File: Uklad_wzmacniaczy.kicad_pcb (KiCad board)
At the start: 4 copper layers, 80 x 120 mm, 85 parts, among them J1 SJ1-3523N, J2 MEM2080-00-128-00-A, J3 Conn_01x10_Pin, U1 OPA2388IDR, U10 AD5162BRMZ10-RL7, U11 AD5162BRMZ10-RL7, U12 LT3094EMSE-TRPBF, U13 Nucleo-H755ZIQ-Morpho, U14 TPS61236PRWLR, U15 LD1117S50TR_SOT223, U2 REF2033QDDCRQ1, U3 AD8421ARMZ, U4 OPA388IDR, U5 AD8421ARMZ, U6 TPD4E1B06DRLR, U7 AD5162BRMZ10-RL7, U8 LT3042EMSE-TRPBF, U9 TPS65135RTER

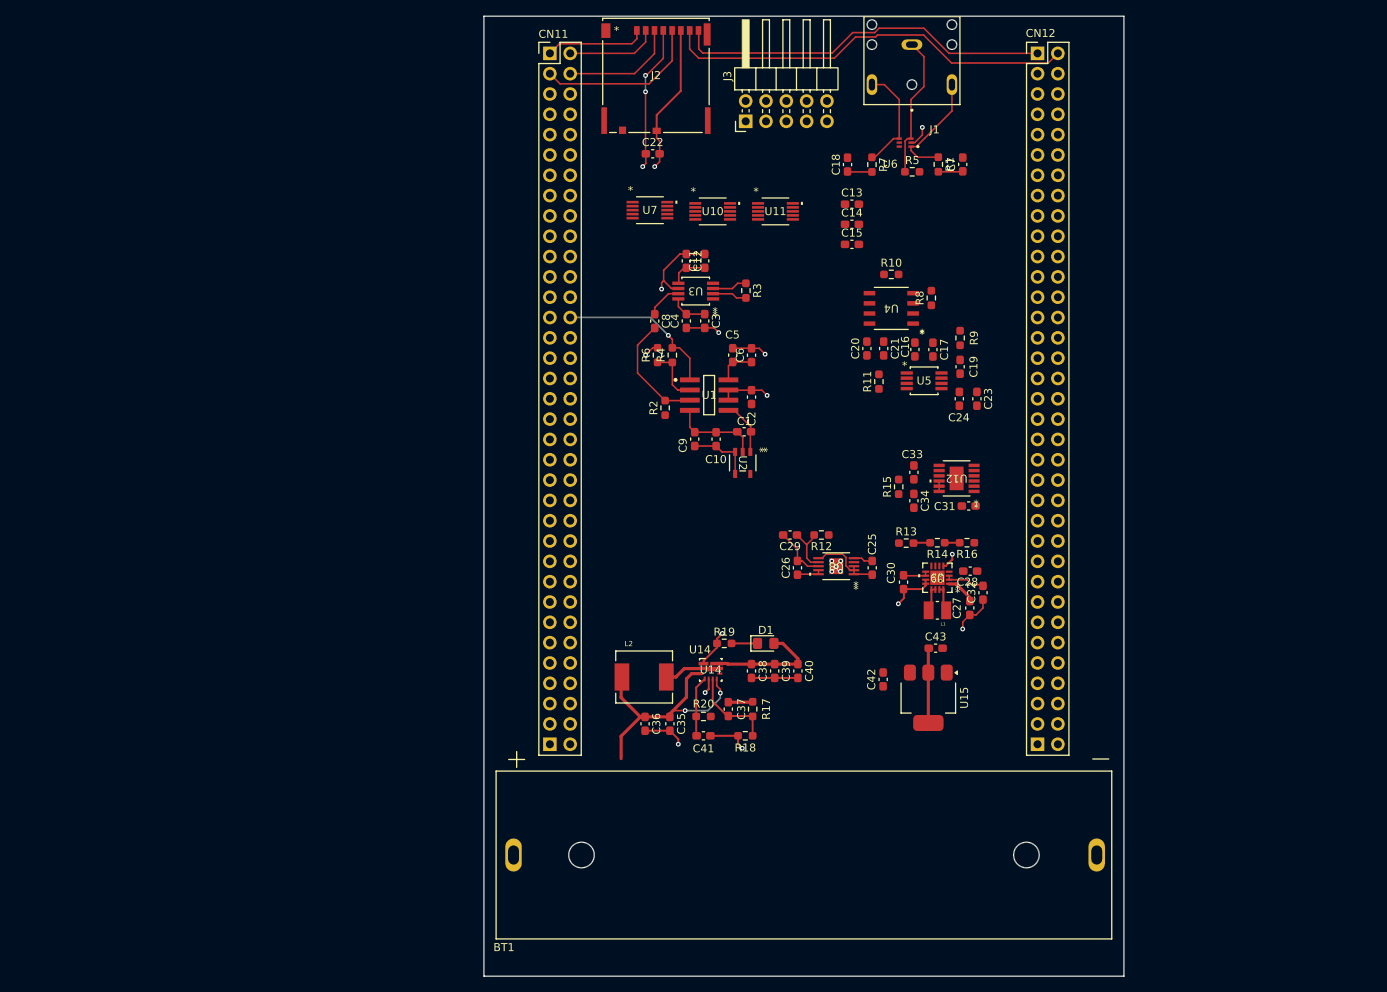
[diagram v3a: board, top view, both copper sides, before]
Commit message: Layout major change, .gitignore added
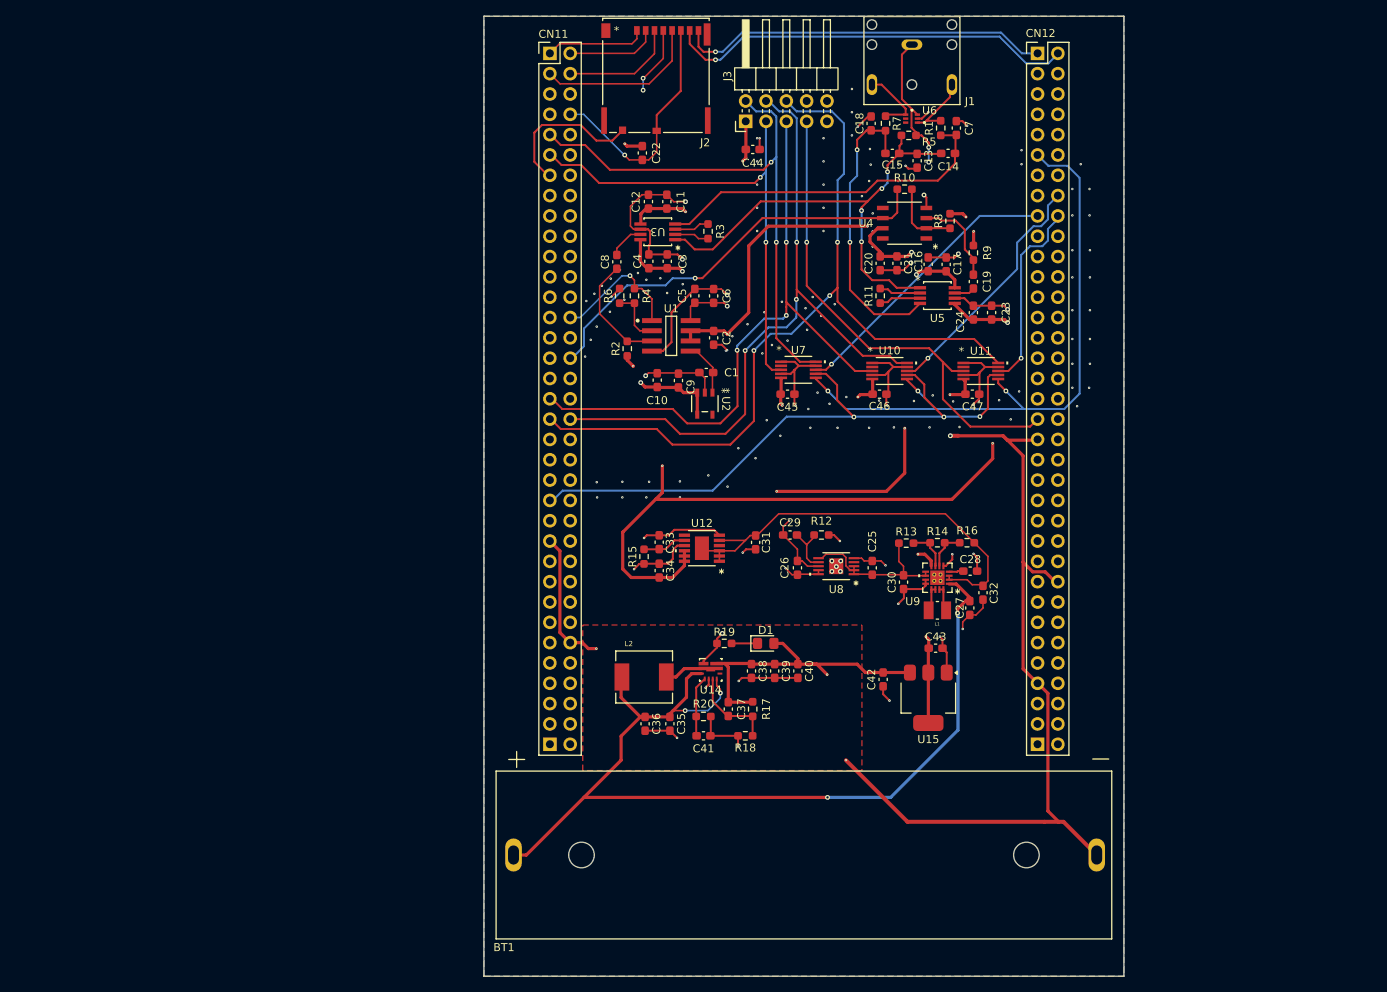
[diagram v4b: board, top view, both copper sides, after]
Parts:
- added C44: 100n, Capacitor_SMD:C_0603_1608Metric_Pad1.08x0.95mm_HandSolder, F.Cu at (139.2, 39.5)
- added C45: 100n, Capacitor_SMD:C_0603_1608Metric_Pad1.08x0.95mm_HandSolder, F.Cu at (143.5, 70.1)
- added C46: 100n, Capacitor_SMD:C_0603_1608Metric_Pad1.08x0.95mm_HandSolder, F.Cu at (155.0, 70.1)
- added C47: 100n, Capacitor_SMD:C_0603_1608Metric_Pad1.08x0.95mm_HandSolder, F.Cu at (166.6, 70.1)
- added NT1: NetTie_2, NetTie:NetTie-2_SMD_Pad0.5mm, F.Cu at (164.4, 75.3)
- moved R15 33.0 mm to (125.6, 90.4)
- moved U12 33.0 mm to (132.8, 89.3)
- moved C33 33.0 mm to (127.5, 88.6)
- moved C34 33.0 mm to (127.5, 92.2)
- moved U11 32.5 mm to (167.7, 67.2)
- moved U10 29.8 mm to (156.3, 67.2)
- moved U7 27.2 mm to (144.9, 67.1)
- moved C31 27.0 mm to (139.6, 88.6), turned to -90 degrees
- moved C14 14.9 mm to (163.6, 40.0)
- moved C15 12.4 mm to (156.7, 40.0), turned to 180 degrees
- moved C23 10.9 mm to (169.1, 59.9), turned to 90 degrees
- moved C24 10.9 mm to (166.8, 59.9), turned to -90 degrees
- moved C16 10.8 mm to (161.1, 53.9)
- moved C20 10.8 mm to (155.1, 53.7)
- moved C21 10.8 mm to (157.2, 53.7)
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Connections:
- U13 pad 1.08: unconnected-(U13-GND-Pad1.08) -> GND
- U13 pad 1.49: unconnected-(U13-GND-Pad1.49) -> GND
- U13 pad 1.60: unconnected-(U13-GND-Pad1.60) -> GND
- U13 pad 2.39: unconnected-(U13-GND-Pad2.39) -> GND
- U13 pad 2.54: unconnected-(U13-GND-Pad2.54) -> GND
- U13 pad 2.63: unconnected-(U13-GND-Pad2.63) -> GND
- U8 pad 11: GND -> GNDA
- U9 pad 17: unconnected-(U9-EPAD-Pad17) -> /Thermal
- U9 pad V: (no net) -> GNDA
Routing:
- net -5VA: track 6.12 -> 145.3 mm, vias 0 -> 4
- net GND: track 41.6 -> 175.5 mm, vias 10 -> 8
- net +5VA: track 15.9 -> 134.1 mm, vias 0 -> 6
- net GNDA: track 55.6 -> 166.3 mm, vias 7 -> 141
- net /SIG_5: track 0.00 -> 104.8 mm, vias 0 -> 3
- net /SIG_3: track 0.00 -> 86.9 mm, vias 0 -> 3
- net +BATT: track 36.8 -> 122.7 mm, vias 2 -> 4
- net /SDI: track 0.00 -> 80.7 mm, vias 0 -> 3
- net /SIG_4: track 0.00 -> 79.5 mm, vias 0 -> 3
- net /CLK: track 0.00 -> 79.2 mm, vias 0 -> 3
- net +1.65VA: track 8.26 -> 85.5 mm, vias 2 -> 6
- net /SIG_1: track 0.00 -> 69.3 mm, vias 0 -> 2
- net /SIG_6: track 0.00 -> 62.9 mm, vias 0 -> 1
- net /SIG_2: track 0.00 -> 61.6 mm, vias 0 -> 2
- net /IN-: track 0.00 -> 59.6 mm, vias 0 -> 4
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- added copper zone on In1.Cu, net +3.3V
- added copper zone on In1.Cu, net +5V
- added copper zone on F.Cu, net GND
- added copper zone on In2.Cu, net GND
- added copper zone on B.Cu, net GNDA
- added copper zone on F.Cu, net GNDA
- added copper zone on In2.Cu, net GNDA

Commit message: Layout and schematic minor changes
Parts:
- added TP1: 3,3V, TestPoint:TestPoint_Pad_D1.5mm, F.Cu at (148.3, 41.3)
- added TP10: POT2, TestPoint:TestPoint_Pad_D1.5mm, F.Cu at (109.0, 42.6)
- added TP11: POT3, TestPoint:TestPoint_Pad_D1.5mm, F.Cu at (109.0, 71.9)
- added TP12: POT4, TestPoint:TestPoint_Pad_D1.5mm, F.Cu at (109.0, 68.3)
- added TP13: POT5, TestPoint:TestPoint_Pad_D1.5mm, F.Cu at (109.0, 75.8)
- added TP14: POT6, TestPoint:TestPoint_Pad_D1.5mm, F.Cu at (181.2, 72.0)
- added TP15: GND, TestPoint:TestPoint_Pad_2.0x2.0mm, F.Cu at (144.2, 112.7)
- added TP16: +BATT, TestPoint:TestPoint_Pad_D1.5mm, F.Cu at (109.3, 112.7)
- added TP17: GNDA, TestPoint:TestPoint_Pad_2.0x2.0mm, F.Cu at (144.6, 77.8)
- added TP2: 5V, TestPoint:TestPoint_Pad_D1.5mm, F.Cu at (148.2, 109.5)
- added TP3: +5V, TestPoint:TestPoint_Pad_D1.5mm, F.Cu at (150.3, 79.9)
- added TP4: -5V, TestPoint:TestPoint_Pad_D1.5mm, F.Cu at (134.3, 79.1)
- added TP5: GNDA, TestPoint:TestPoint_Pad_2.0x2.0mm, F.Cu at (168.6, 107.7)
- added TP6: 1,65V, TestPoint:TestPoint_Pad_D1.5mm, F.Cu at (168.0, 46.0)
- added TP7: ADC1, TestPoint:TestPoint_Pad_D1.5mm, F.Cu at (109.0, 59.2)
- added TP8: ADC2, TestPoint:TestPoint_Pad_D1.5mm, F.Cu at (109.0, 64.3)
- added TP9: POT1, TestPoint:TestPoint_Pad_D1.5mm, F.Cu at (109.0, 37.8)
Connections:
- U9 pad 17: /Thermal -> GNDA
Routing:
- net +BATT: track 122.7 -> 137.6 mm
- net /TO_ADC2: track 52.6 -> 66.4 mm
- net /SIG_3: track 86.9 -> 94.9 mm
- net /TO_ADC1: track 16.9 -> 24.7 mm
- net /SIG_6: track 62.9 -> 70.2 mm
- net +5V: track 39.5 -> 46.8 mm
- net /SIG_2: track 61.6 -> 68.0 mm, vias 2 -> 3
- net /SIG_5: track 104.8 -> 110.7 mm
- net /SIG_4: track 79.5 -> 85.4 mm
- net -5VA: track 145.3 -> 150.5 mm
- net /SIG_1: track 69.3 -> 74.2 mm, vias 2 -> 3
- net +5VA: track 134.1 -> 137.5 mm
- net +1.65VA: track 85.5 -> 88.4 mm
- net +3.3V: track 57.1 -> 58.6 mm, vias 11 -> 12
- net GNDA: track 166.3 -> 166.1 mm, vias 141 -> 143
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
